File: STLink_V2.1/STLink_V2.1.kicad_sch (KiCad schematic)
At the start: 22 parts, among them J1 USB_C_Receptacle, J2 Conn_01x04_Pin, U1 STM32F103C8Tx, U2 RT9193-33GB, Y1 Crystal_GND24_Small

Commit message: Complete Schematic
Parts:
- removed R1: 1M, IVS_FOOTPRINTS:R_0603, symbol Thu_vien_kicad:R
- added C1: 10uF, IVS_FOOTPRINTS:C_0603, symbol Device:C
- added C2: 1uF, IVS_FOOTPRINTS:C_0603, symbol Device:C
- added C3: 100nF, IVS_FOOTPRINTS:C_0603, symbol Device:C
- added C4: 33pF, IVS_FOOTPRINTS:C_0603, symbol Device:C
- added C5: 10pF, IVS_FOOTPRINTS:C_0603, symbol Device:C
- added J1: Conn_01x05_Male, Connector_PinHeader_2.54mm:PinHeader_1x06_P2.54mm_Vertical, symbol Connector:Conn_01x06_Male
- added J3, J4: Conn_01x04_Pin, Connector_PinHeader_2.54mm:PinHeader_1x04_P2.54mm_Vertical, symbol Connector:Conn_01x04_Pin
- added LE2, LE3, LE4: Led, IVS_FOOTPRINTS:LED_0603, symbol IVS_SYMBOLS:Led
- added R1: 100, IVS_FOOTPRINTS:R_0603, symbol Device:R
- added R11, R13, R14: 1k, IVS_FOOTPRINTS:R_0603, symbol Device:R
- added R7: 100, IVS_FOOTPRINTS:R_0603, symbol Thu_vien_kicad:R
- added R8, R9: 10K, IVS_FOOTPRINTS:R_0603, symbol Device:R
- added U1: ESP32-WROOM-32UE, IVS_FOOTPRINTS:ESP32-WROOM-32E, symbol RF_Module:ESP32-WROOM-32D
- added Z1: D_Zener, IVS_FOOTPRINTS:Package-Diode-D_MiniMELF, symbol IVS_SYMBOLS:D_Zener
- C3: value 1uF -> 100nF
- J2: footprint (none) -> Connector_PinHeader_2.54mm:PinHeader_1x04_P2.54mm_Vertical
- Y1: footprint IVS_FOOTPRINTS:Crystal_3225_4P_3.2x2.6mm -> IVS_FOOTPRINTS:Crystal-SMD-4P-3.2x2.6mm-3225
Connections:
- net +3V3: now also J2.3 (Pin_3), U1.1 (VBAT), C1.1, C2.1, C3.1, C4.1, C5.1, J1.6 (Pin_6), J3.4 (Pin_4), R11.1, R13.1, R14.1, U1.2 (VDD), Z1.2; no longer J2.4 (Pin_4)
- net +5V: now also J4.4 (Pin_4)
- net GND: now also J2.4 (Pin_4), C1.2, C2.2, C3.2, C4.2, C5.2, J1.1 (Pin_1), J3.3 (Pin_3), J4.3 (Pin_3), R8.1, R9.1, U1.1 (GND), U1.15 (GND), U1.38 (GND), U1.39 (GND), Z1.1; no longer J2.3 (Pin_3)
- net RST: now also J1.2 (Pin_2), U1.3 (EN)
- net ST_SWCLK: now also J2.1 (Pin_1); no longer J2.2 (Pin_2)
- net ST_SWDIO: now also J2.2 (Pin_2); no longer J2.1 (Pin_1)
- net T_TXD: now reaches U1.12 (PA2)
- net T_TXD: now also J4.2 (Pin_2), LE2.2
- net T_RXD: now reaches U1.13 (PA3)
- net T_RXD: now also J4.1 (Pin_1)
- net T_SWCLK: now reaches U1.15 (PA5)
- net T_SWCLK: now also U1.26 (PB13), J3.1 (Pin_1)
- net at U1.2 (PC13): now also R8.2
- net at U1.25 (PB12): now also R7.1
- net T_SWDIO: now reaches U1.27 (PB14)
- net T_SWDIO: now also J3.2 (Pin_2), LE3.2, LE4.1, R7.2
- net at U1.3 (PC14): now also R9.2
- net ESP_RXD: now reaches U1.30 (PA9)
- net ESP_RXD: now also R1.2
- net ESP_TXD: now reaches U1.31 (PA10)
- net ESP_TXD: now also U1.28 (IO17)
- new net: LE4.2, R14.2
- new net: LE3.1, R13.2
- new net: R1.1, U1.27 (IO16)
- new net: LE2.1, R11.2
- new net BOOT: J1.5 (Pin_5), U1.25 (IO0)
- new net RX: J1.4 (Pin_4), U1.34 (RXD0/IO3)
- new net TX: J1.3 (Pin_3), U1.35 (TXD0/IO1)
- no-connect marks 5 -> 49
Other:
- moved on the sheet: C1, C10, C2, C3, C4, C5, C6, C7, C8, C9, J1, J2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

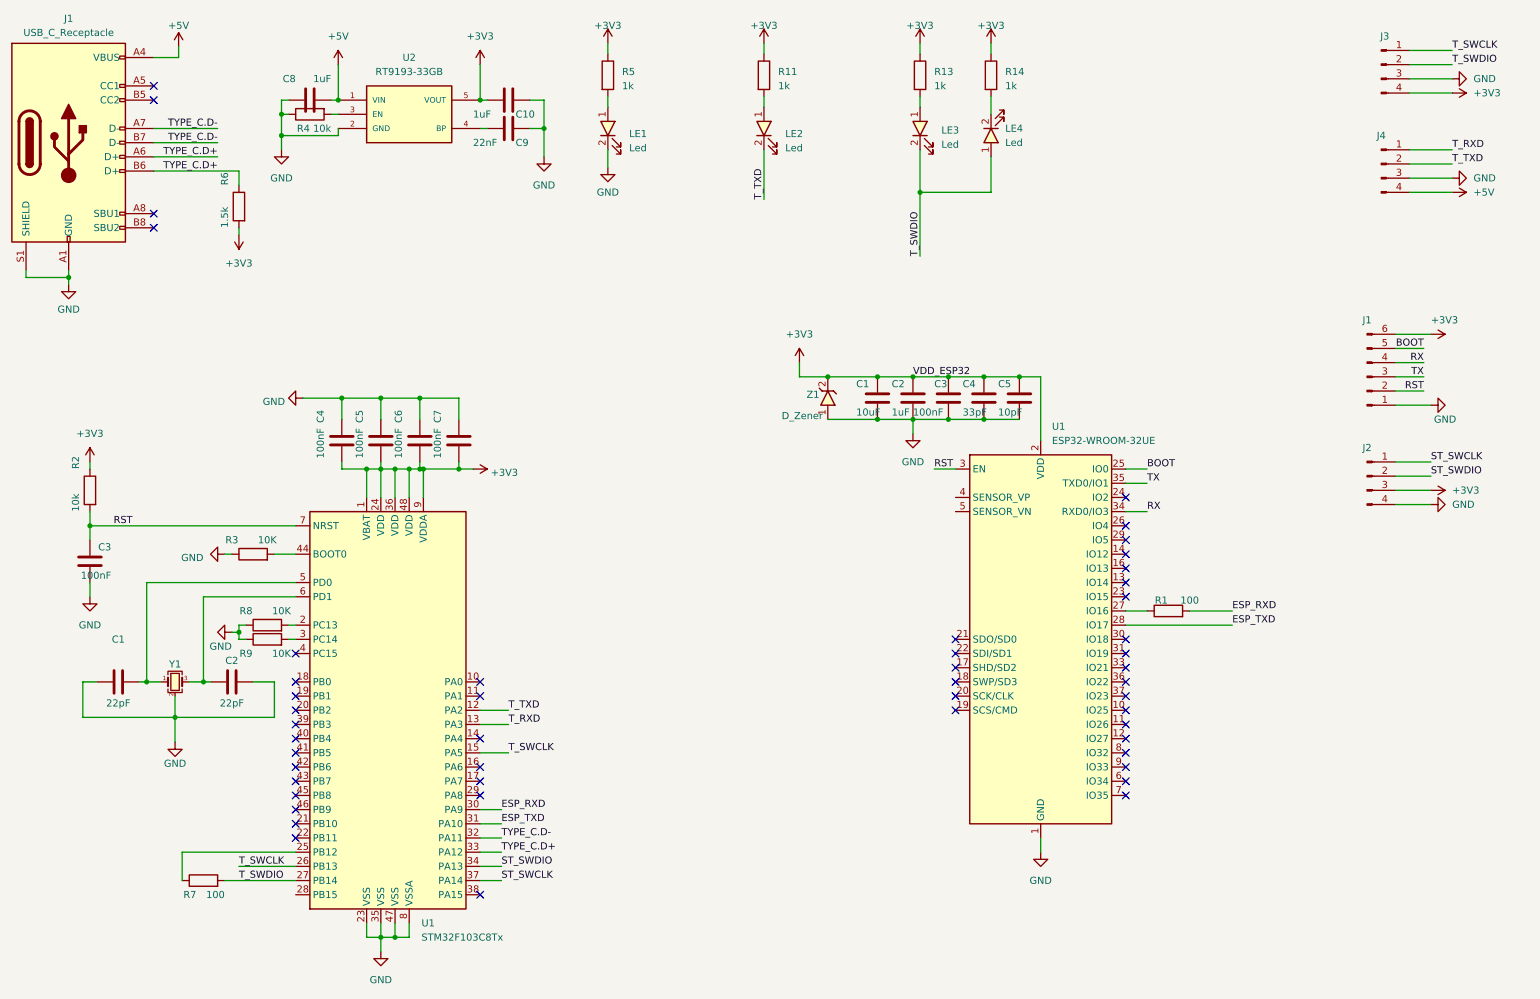
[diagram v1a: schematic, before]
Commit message: Delete ESP32
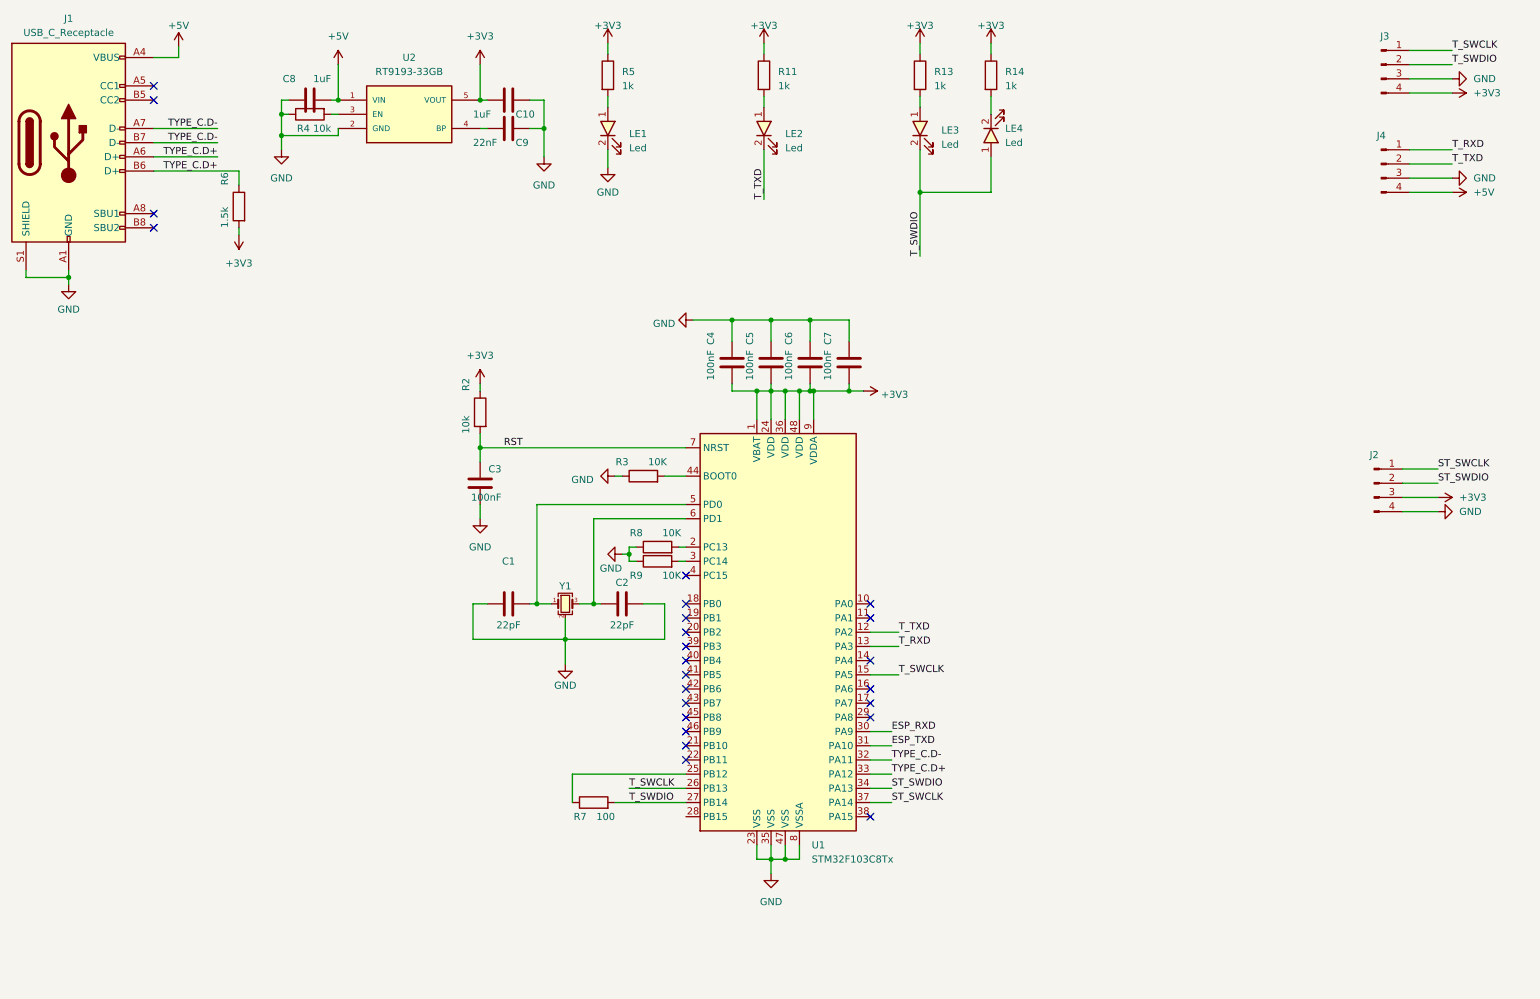
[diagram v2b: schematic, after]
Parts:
- removed C1: 10uF, IVS_FOOTPRINTS:C_0603, symbol Device:C
- removed C2: 1uF, IVS_FOOTPRINTS:C_0603, symbol Device:C
- removed C3: 100nF, IVS_FOOTPRINTS:C_0603, symbol Device:C
- removed C4: 33pF, IVS_FOOTPRINTS:C_0603, symbol Device:C
- removed C5: 10pF, IVS_FOOTPRINTS:C_0603, symbol Device:C
- removed J1: Conn_01x05_Male, Connector_PinHeader_2.54mm:PinHeader_1x06_P2.54mm_Vertical, symbol Connector:Conn_01x06_Male
- removed R1: 100, IVS_FOOTPRINTS:R_0603, symbol Device:R
- removed U1: ESP32-WROOM-32UE, IVS_FOOTPRINTS:ESP32-WROOM-32E, symbol RF_Module:ESP32-WROOM-32D
- removed Z1: D_Zener, IVS_FOOTPRINTS:Package-Diode-D_MiniMELF, symbol IVS_SYMBOLS:D_Zener
- J2, J3, J4: footprint Connector_PinHeader_2.54mm:PinHeader_1x04_P2.54mm_Vertical -> IVS_FOOTPRINTS:Conn-Horz-SMD-4P-2.54mm-PinHeader
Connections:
- no-connect marks 49 -> 24
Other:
- moved on the sheet: C1, C2, C3, C4, C5, C6, C7, J2, R2, R3, R7, R8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
